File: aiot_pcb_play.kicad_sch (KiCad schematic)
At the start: 10 parts, among them J1 10_pin_swd_connector, J2 Tag-Connect, U1 BC833M, U2 16_pin_header, U3 ITM-DYPA-B-02

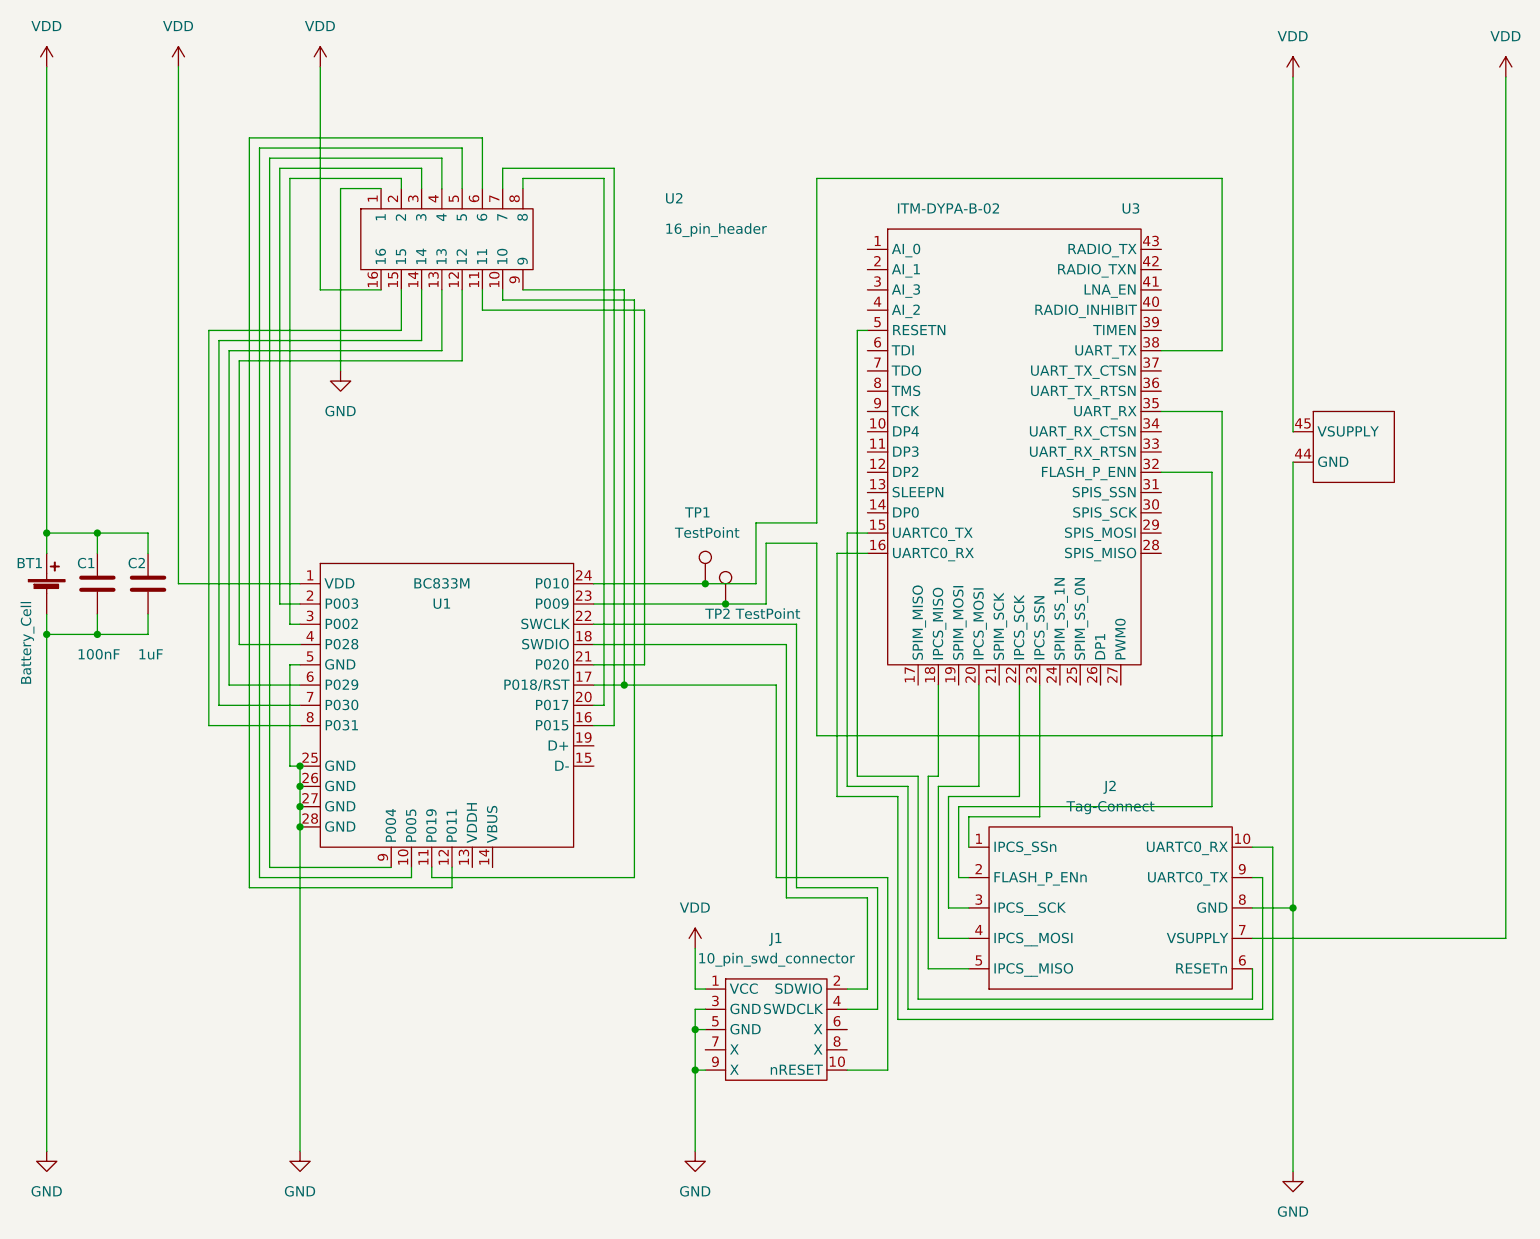
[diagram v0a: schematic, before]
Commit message: #1 Fix added missing flow control connections to the Schematics
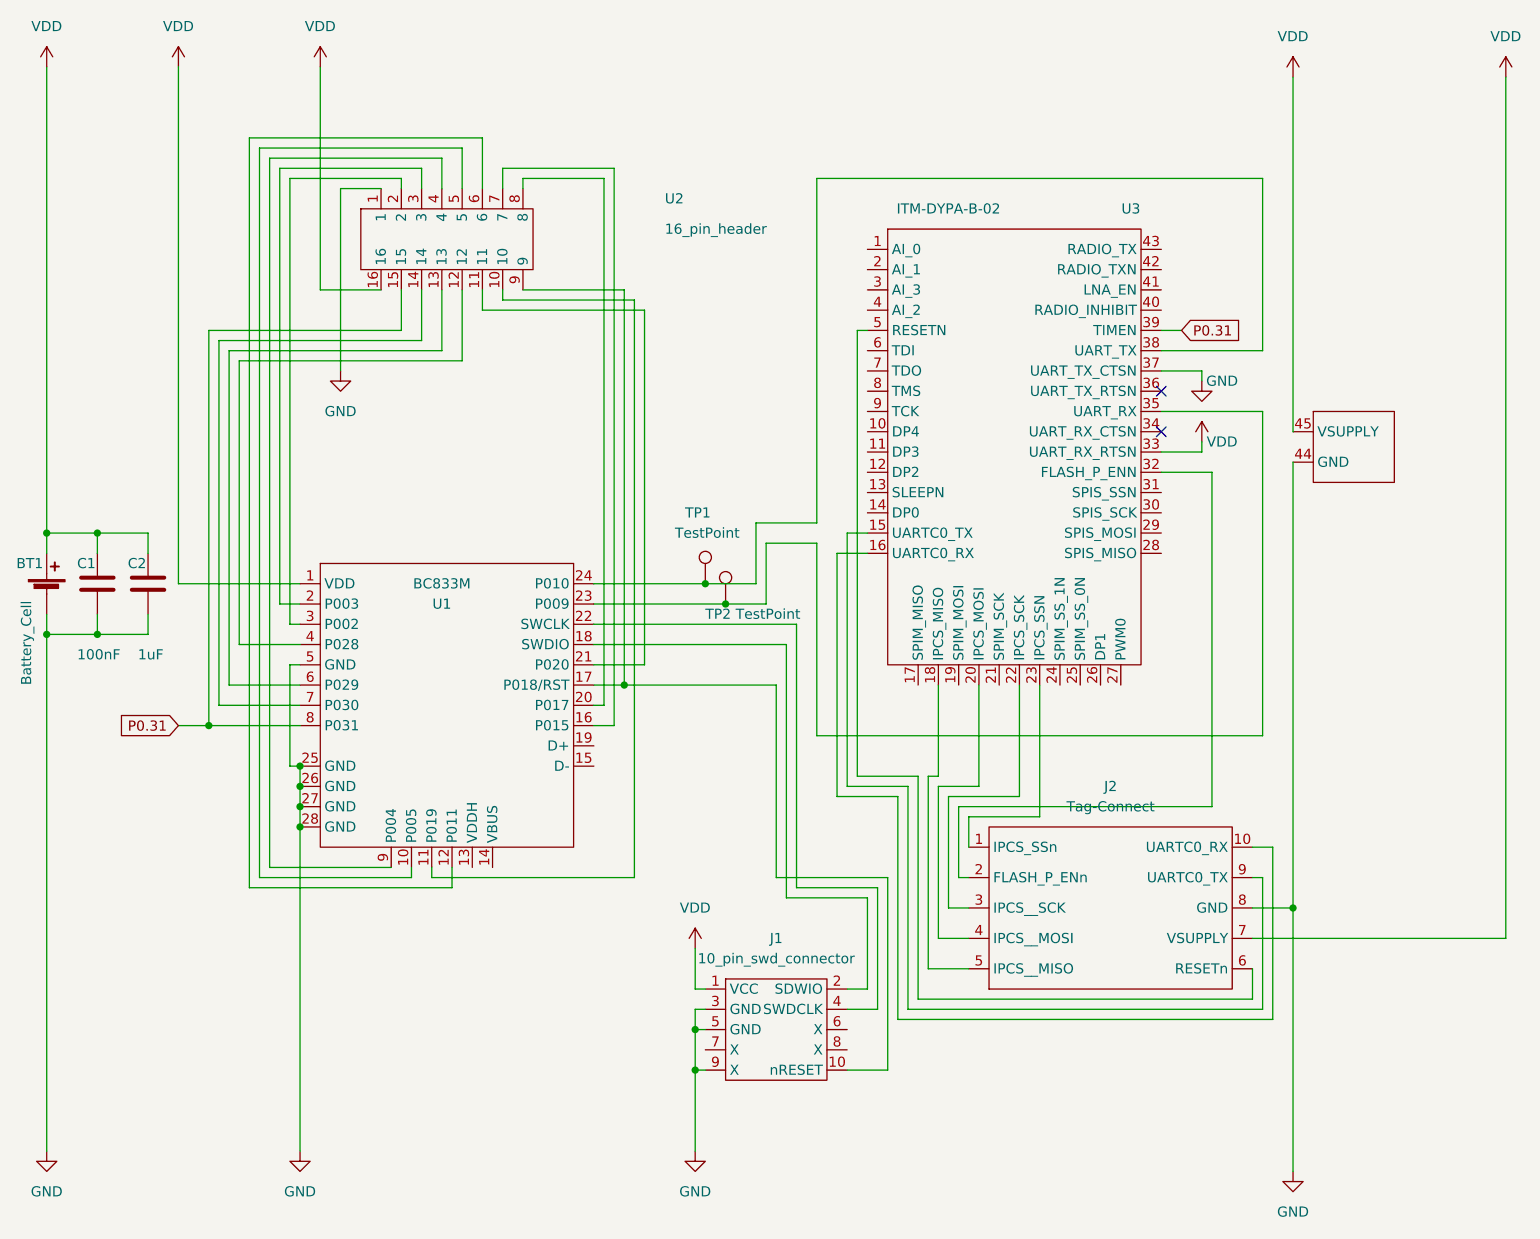
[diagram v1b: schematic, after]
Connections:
- net GND: now also U3.37 (UART_TX_CTSN)
- net VDD: now also U3.33 (UART_RX_RTSN)
- net P0.31: now reaches U1.8 (P031), U2.15
- net P0.31: now also U3.39 (TIMEN)
- no-connect marks 0 -> 2
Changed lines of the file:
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@@
   (junction (at 48.26 114.3) (diameter 0) (color 0 0 0 0)
   )
+  (junction (at 36.83 109.22) (diameter 0) (color 0 0 0 0)
+  )
   (junction (at 22.86 85.09) (diameter 0) (color 0 0 0 0)
   )
@@
   (junction (at 48.26 116.84) (diameter 0) (color 0 0 0 0)
   )
+  (no_connect (at 156.21 72.39))
+  (no_connect (at 156.21 67.31))
+  (wire (pts (xy 33.02 109.22) (xy 36.83 109.22))
+    (stroke (width 0) (type default) (color 0 0 0 0))
+  )
   (wire (pts (xy 172.72 27.94) (xy 172.72 72.39))
     (stroke (width 0) (type default) (color 0 0 0 0))
@@
     (stroke (width 0) (type default) (color 0 0 0 0))
   )
-  (wire (pts (xy 113.03 40.64) (xy 163.83 40.64))
+  (wire (pts (xy 113.03 40.64) (xy 168.91 40.64))
     (stroke (width 0) (type default) (color 0 0 0 0))
   )
@@
     (stroke (width 0) (type default) (color 0 0 0 0))
   )
+  (wire (pts (xy 161.29 64.77) (xy 161.29 66.04))
+    (stroke (width 0) (type default) (color 0 0 0 0))
+  )
   (wire (pts (xy 58.42 41.91) (xy 53.34 41.91))
     (stroke (width 0) (type default) (color 0 0 0 0))
@@
     (stroke (width 0) (type default) (color 0 0 0 0))
   )
-  (wire (pts (xy 163.83 69.85) (xy 156.21 69.85))
+  (wire (pts (xy 168.91 69.85) (xy 156.21 69.85))
     (stroke (width 0) (type default) (color 0 0 0 0))
   )
@@
     (stroke (width 0) (type default) (color 0 0 0 0))
   )
-  (wire (pts (xy 113.03 110.49) (xy 163.83 110.49))
+  (wire (pts (xy 113.03 110.49) (xy 168.91 110.49))
     (stroke (width 0) (type default) (color 0 0 0 0))
   )
@@
     (stroke (width 0) (type default) (color 0 0 0 0))
   )
-  (wire (pts (xy 163.83 62.23) (xy 156.21 62.23))
+  (wire (pts (xy 168.91 62.23) (xy 156.21 62.23))
     (stroke (width 0) (type default) (color 0 0 0 0))
   )
@@
     (stroke (width 0) (type default) (color 0 0 0 0))
   )
+  (wire (pts (xy 156.21 74.93) (xy 161.29 74.93))
+    (stroke (width 0) (type default) (color 0 0 0 0))
+  )
   (wire (pts (xy 110.49 96.52) (xy 110.49 129.54))
     (stroke (width 0) (type default) (color 0 0 0 0))
@@
     (stroke (width 0) (type default) (color 0 0 0 0))
   )
+  (wire (pts (xy 156.21 59.69) (xy 158.75 59.69))
+    (stroke (width 0) (type default) (color 0 0 0 0))
+  )
   (wire (pts (xy 128.27 135.89) (xy 128.27 116.84))
     (stroke (width 0) (type default) (color 0 0 0 0))
@@
     (stroke (width 0) (type default) (color 0 0 0 0))
   )
+  (wire (pts (xy 156.21 64.77) (xy 161.29 64.77))
+    (stroke (width 0) (type default) (color 0 0 0 0))
+  )
   (wire (pts (xy 105.41 91.44) (xy 105.41 83.82))
     (stroke (width 0) (type default) (color 0 0 0 0))
@@
     (stroke (width 0) (type default) (color 0 0 0 0))
   )
-  (wire (pts (xy 163.83 40.64) (xy 163.83 62.23))
+  (wire (pts (xy 168.91 40.64) (xy 168.91 62.23))
     (stroke (width 0) (type default) (color 0 0 0 0))
   )
@@
     (stroke (width 0) (type default) (color 0 0 0 0))
   )
-  (wire (pts (xy 163.83 110.49) (xy 163.83 69.85))
+  (wire (pts (xy 168.91 110.49) (xy 168.91 69.85))
     (stroke (width 0) (type default) (color 0 0 0 0))
   )
@@
     (stroke (width 0) (type default) (color 0 0 0 0))
   )
+  (wire (pts (xy 161.29 74.93) (xy 161.29 73.66))
+    (stroke (width 0) (type default) (color 0 0 0 0))
+  )
   (wire (pts (xy 128.27 116.84) (xy 133.35 116.84))
     (stroke (width 0) (type default) (color 0 0 0 0))
@@
   (wire (pts (xy 22.86 85.09) (xy 16.51 85.09))
     (stroke (width 0) (type default) (color 0 0 0 0))
+  )
+  (global_label "P0.31" (shape input) (at 158.75 59.69 0) (fields_autoplaced)
+    (effects (font (size 1.27 1.27)) (justify left))
+    (property "Intersheet References" "${INTERSHEET_REFS}" (id 0) (at 166.6664 59.6106 0)
+      (effects (font (size 1.27 1.27)) (justify left) hide)
+    )
+  )
+  (global_label "P0.31" (shape input) (at 33.02 109.22 180) (fields_autoplaced)
+    (effects (font (size 1.27 1.27)) (justify right))
+    (property "Intersheet References" "${INTERSHEET_REFS}" (id 0) (at 25.1036 109.2994 0)
+      (effects (font (size 1.27 1.27)) (justify right) hide)
+    )
   )
   (symbol (lib_id "heat_humidity_mesh_lib:16_pin_header") (at 67.31 48.26 0) (unit 1)
@@
     )
     (property "Datasheet" "" (id 3) (at 50.8 26.67 0)
+      (effects (font (size 1.27 1.27)) hide)
+    )
+    (pin "1")
+  )
+  (symbol (lib_id "power:GND") (at 161.29 66.04 0) (unit 1)
+    (in_bom yes) (on_board yes)
+    (property "Reference" "#PWR?" (id 0) (at 161.29 72.39 0)
+      (effects (font (size 1.27 1.27)) hide)
+    )
+    (property "Value" "GND" (id 1) (at 163.83 66.04 0))
+    (property "Footprint" "" (id 2) (at 161.29 66.04 0)
+      (effects (font (size 1.27 1.27)) hide)
+    )
+    (property "Datasheet" "" (id 3) (at 161.29 66.04 0)
       (effects (font (size 1.27 1.27)) hide)
     )
@@
     (pin "1")
   )
+  (symbol (lib_id "power:VDD") (at 161.29 73.66 0) (unit 1)
+    (in_bom yes) (on_board yes)
+    (property "Reference" "#PWR?" (id 0) (at 161.29 77.47 0)
+      (effects (font (size 1.27 1.27)) hide)
+    )
+    (property "Value" "VDD" (id 1) (at 163.83 73.66 0))
+    (property "Footprint" "" (id 2) (at 161.29 73.66 0)
+      (effects (font (size 1.27 1.27)) hide)
+    )
+    (property "Datasheet" "" (id 3) (at 161.29 73.66 0)
+      (effects (font (size 1.27 1.27)) hide)
+    )
+    (pin "1")
+  )
   (symbol (lib_id "heat_humidity_mesh_lib:10_pin_swd_connector") (at 107.95 147.32 0) (unit 1)
     (in_bom yes) (on_board yes) (fields_autoplaced)
@@
       (reference "#PWR011") (unit 1) (value "VDD") (footprint "")
     )
+    (path "/86dde403-4883-4242-bcef-5f73f9e5ffdd"
+      (reference "#PWR?") (unit 1) (value "GND") (footprint "")
+    )
+    (path "/efcf8b8e-b4a4-447f-9f1f-480ef2d2869e"
+      (reference "#PWR?") (unit 1) (value "VDD") (footprint "")
+    )
     (path "/31f48bfa-414a-4ea3-87a1-96ca97a99923"
